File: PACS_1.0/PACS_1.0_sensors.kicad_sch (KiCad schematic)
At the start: 5 parts, among them J1 Conn_01x04_Socket, U4 LTR-303ALS-01, U5 MCP9700Ax-ETT

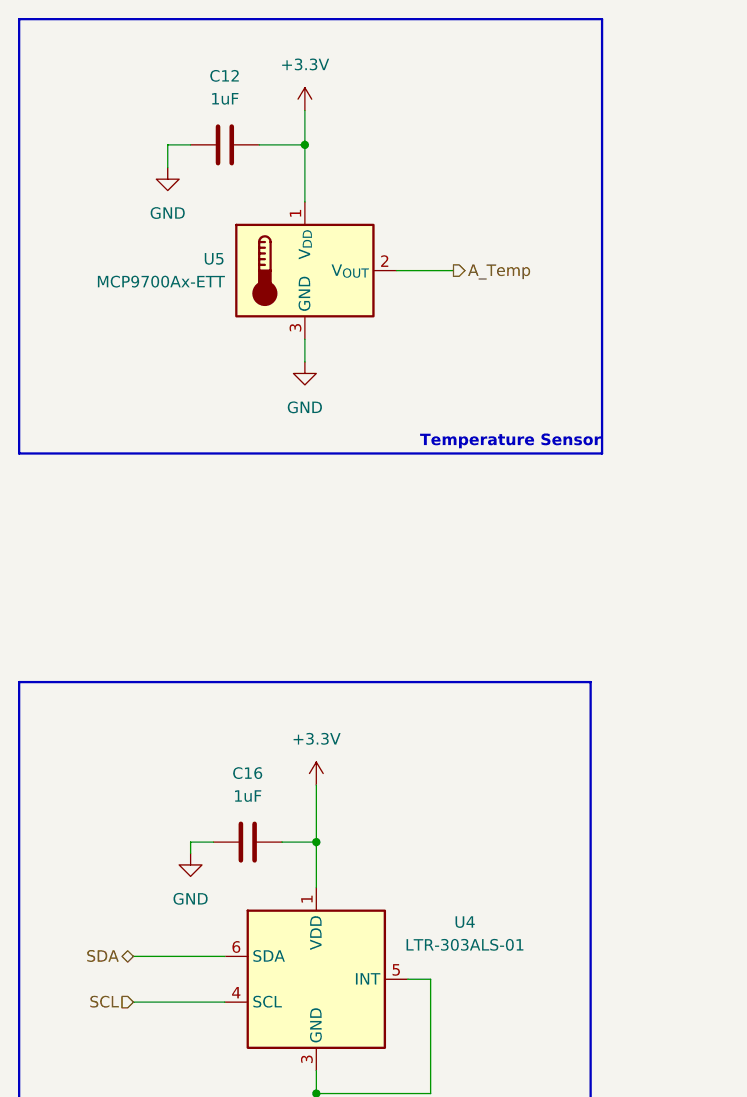
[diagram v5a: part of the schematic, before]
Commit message: Changed reference for Components
C8 to C2 (AS EXAMPLE)
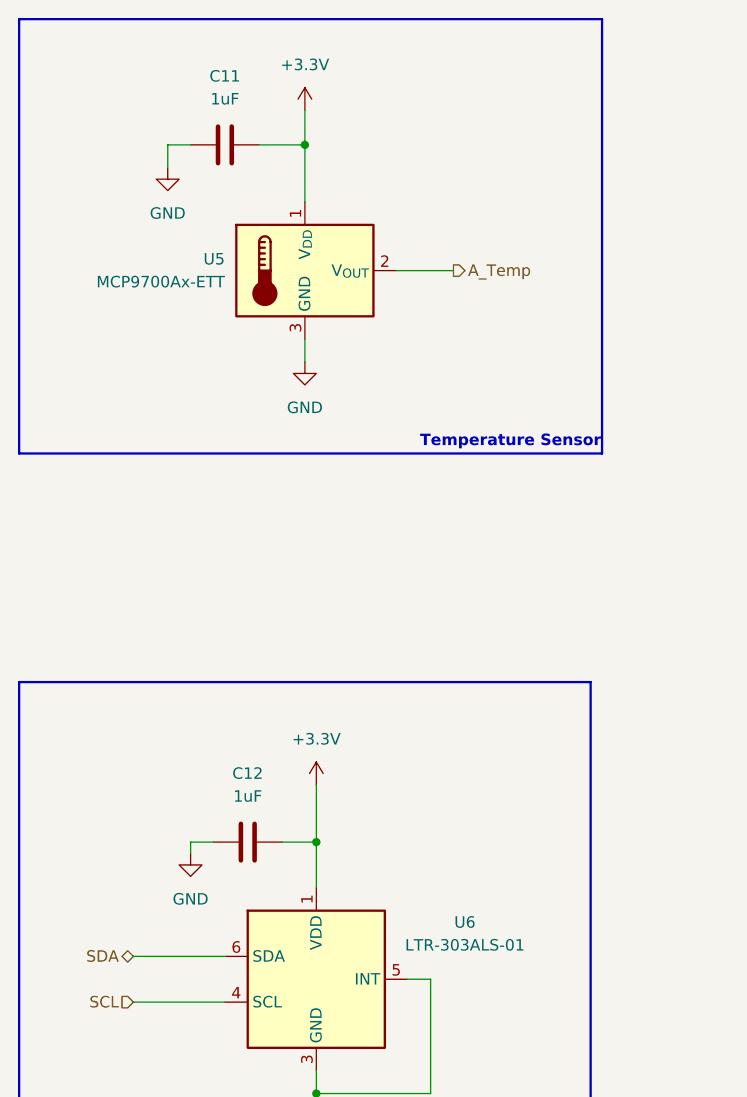
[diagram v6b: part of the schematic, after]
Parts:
- renumbered C12 to C11, C16 to C12, U4 to U6
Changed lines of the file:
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@@
 		(dnp no)
 		(fields_autoplaced yes)
-		(property "Reference" "C16"
+		(property "Reference" "C12"
 			(at 88.9 111.76 90)
 			(effects
@@
 			(project ""
 				(path "/6996cbc8-fffb-40fd-8350-2bb7d19e6e7a/630878d5-00b9-479f-bc27-1c377eb1e012"
-					(reference "C16")
+					(reference "C12")
 					(unit 1)
 				)
@@
 		(dnp no)
 		(fields_autoplaced yes)
-		(property "Reference" "C12"
+		(property "Reference" "C11"
 			(at 86.36 34.29 90)
 			(effects
@@
 			(project "PACS_1.0"
 				(path "/6996cbc8-fffb-40fd-8350-2bb7d19e6e7a/630878d5-00b9-479f-bc27-1c377eb1e012"
-					(reference "C12")
+					(reference "C11")
 					(unit 1)
 				)
@@
 		(dnp no)
 		(fields_autoplaced yes)
-		(property "Reference" "#PWR020"
+		(property "Reference" "#PWR022"
 			(at 95.25 41.91 0)
 			(effects
@@
 			(project "PACS_1.0"
 				(path "/6996cbc8-fffb-40fd-8350-2bb7d19e6e7a/630878d5-00b9-479f-bc27-1c377eb1e012"
-					(reference "#PWR020")
+					(reference "#PWR022")
 					(unit 1)
 				)
@@
 		(dnp no)
 		(fields_autoplaced yes)
-		(property "Reference" "#PWR034"
+		(property "Reference" "#PWR020"
 			(at 80.01 50.8 0)
 			(effects
@@
 			(project "PACS_1.0"
 				(path "/6996cbc8-fffb-40fd-8350-2bb7d19e6e7a/630878d5-00b9-479f-bc27-1c377eb1e012"
-					(reference "#PWR034")
+					(reference "#PWR020")
 					(unit 1)
 				)
@@
 		(dnp no)
 		(fields_autoplaced yes)
-		(property "Reference" "#PWR019"
+		(property "Reference" "#PWR023"
 			(at 95.25 72.39 0)
 			(effects
@@
 			(project "PACS_1.0"
 				(path "/6996cbc8-fffb-40fd-8350-2bb7d19e6e7a/630878d5-00b9-479f-bc27-1c377eb1e012"
-					(reference "#PWR019")
+					(reference "#PWR023")
 					(unit 1)
 				)
@@
 		(dnp no)
 		(fields_autoplaced yes)
-		(property "Reference" "#PWR017"
+		(property "Reference" "#PWR025"
 			(at 96.52 157.48 0)
 			(effects
@@
 			(project ""
 				(path "/6996cbc8-fffb-40fd-8350-2bb7d19e6e7a/630878d5-00b9-479f-bc27-1c377eb1e012"
-					(reference "#PWR017")
+					(reference "#PWR025")
 					(unit 1)
 				)
@@
 		(dnp no)
 		(fields_autoplaced yes)
-		(property "Reference" "#PWR018"
+		(property "Reference" "#PWR021"
 			(at 82.55 127 0)
 			(effects
@@
 			(project "PACS_1.0"
 				(path "/6996cbc8-fffb-40fd-8350-2bb7d19e6e7a/630878d5-00b9-479f-bc27-1c377eb1e012"
-					(reference "#PWR018")
+					(reference "#PWR021")
 					(unit 1)
 				)
@@
 		(dnp no)
 		(fields_autoplaced yes)
-		(property "Reference" "#PWR016"
+		(property "Reference" "#PWR024"
 			(at 96.52 116.84 0)
 			(effects
@@
 			(project ""
 				(path "/6996cbc8-fffb-40fd-8350-2bb7d19e6e7a/630878d5-00b9-479f-bc27-1c377eb1e012"
-					(reference "#PWR016")
+					(reference "#PWR024")
 					(unit 1)
 				)
@@
 		(dnp no)
 		(fields_autoplaced yes)
-		(property "Reference" "#PWR022"
+		(property "Reference" "#PWR027"
 			(at 196.85 99.06 0)
 			(effects
@@
 			(project "PACS_1.0"
 				(path "/6996cbc8-fffb-40fd-8350-2bb7d19e6e7a/630878d5-00b9-479f-bc27-1c377eb1e012"
-					(reference "#PWR022")
+					(reference "#PWR027")
 					(unit 1)
 				)
@@
 		(dnp no)
 		(fields_autoplaced yes)
-		(property "Reference" "#PWR021"
+		(property "Reference" "#PWR026"
 			(at 196.85 88.9 0)
 			(effects
@@
 			(project "PACS_1.0"
 				(path "/6996cbc8-fffb-40fd-8350-2bb7d19e6e7a/630878d5-00b9-479f-bc27-1c377eb1e012"
-					(reference "#PWR021")
+					(reference "#PWR026")
 					(unit 1)
 				)
@@
 		(dnp no)
 		(fields_autoplaced yes)
-		(property "Reference" "U4"
+		(property "Reference" "U6"
 			(at 113.03 128.3014 0)
 			(effects
@@
 			(project ""
 				(path "/6996cbc8-fffb-40fd-8350-2bb7d19e6e7a/630878d5-00b9-479f-bc27-1c377eb1e012"
-					(reference "U4")
-					(unit 1)
-				)
+					(reference "U6")
+					(unit 1)
+				)

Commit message: Updated footprints for caps and resistors
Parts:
- C11, C12: footprint (none) -> Capacitor_SMD:C_0603_1608Metric
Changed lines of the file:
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@@
 			)
 		)
-		(property "Footprint" ""
+		(property "Footprint" "Capacitor_SMD:C_0603_1608Metric"
 			(at 92.71 118.4148 0)
 			(effects
@@
 			)
 		)
-		(property "Footprint" ""
+		(property "Footprint" "Capacitor_SMD:C_0603_1608Metric"
 			(at 90.17 40.9448 0)
 			(effects

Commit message: Started the PCB design
added several footprints, need to find footprint for Xbee, need to add traces for GND and power
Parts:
- J1: footprint (none) -> Connector_PinSocket_2.54mm:PinSocket_1x04_P2.54mm_Vertical
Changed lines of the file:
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@@
 			)
 		)
-		(property "Footprint" ""
+		(property "Footprint" "Connector_PinSocket_2.54mm:PinSocket_1x04_P2.54mm_Vertical"
 			(at 217.17 85.09 0)
 			(effects
